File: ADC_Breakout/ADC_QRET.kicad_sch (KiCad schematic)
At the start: 33 parts, among them J1 Screw_Terminal_01x03, J2 Screw_Terminal_01x04, J3 Screw_Terminal_01x04, J4 Screw_Terminal_01x04, J5 Screw_Terminal_01x04, U1 ESP32-S3-DEVKITC-1-N8R2

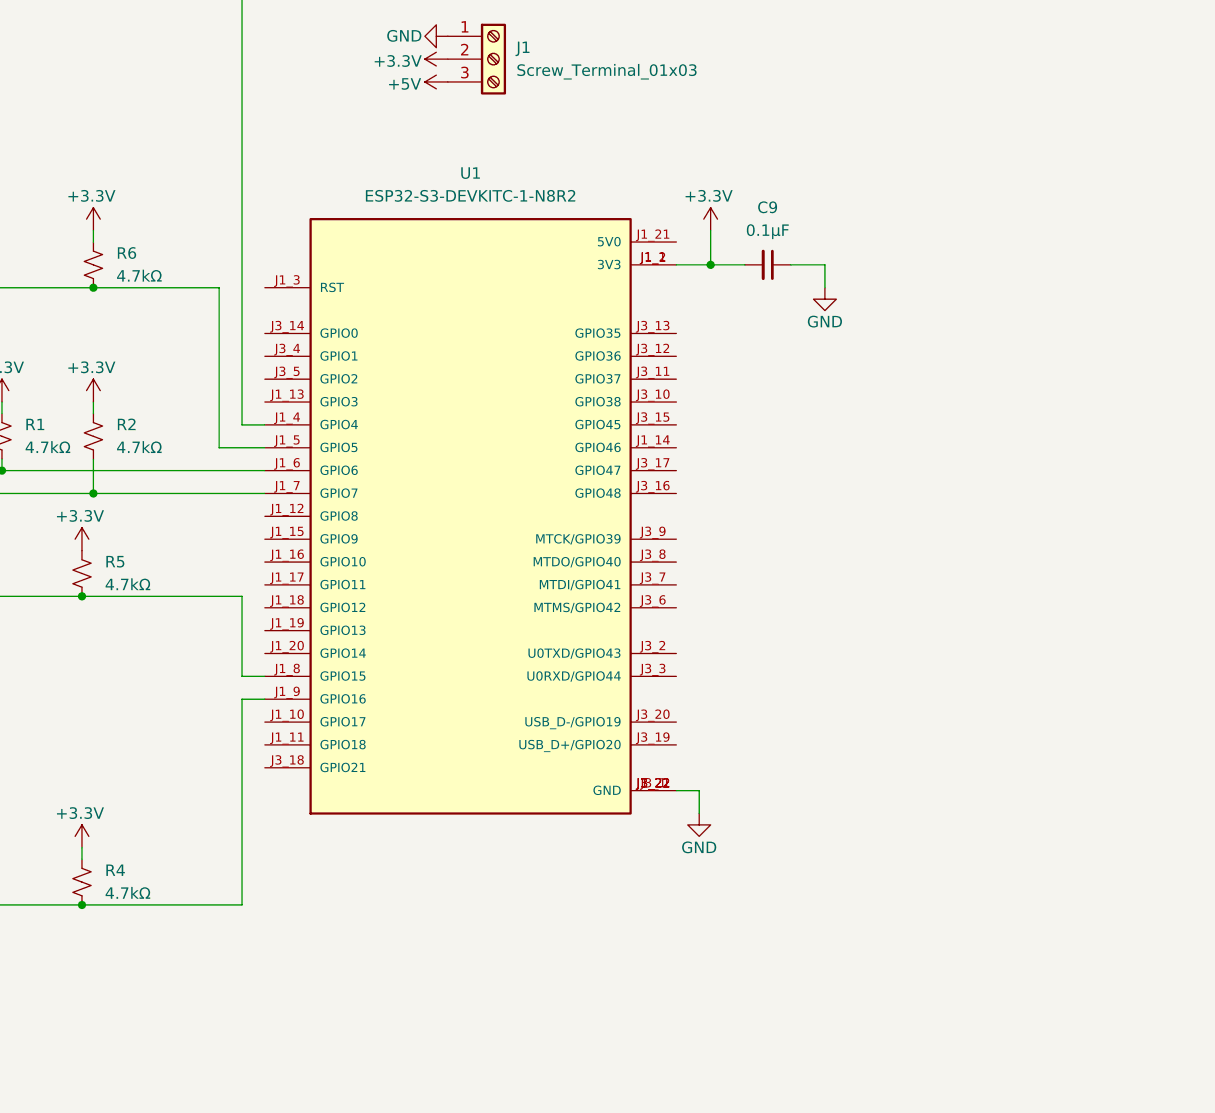
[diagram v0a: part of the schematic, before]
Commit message: Added ESP32 IO Terminals
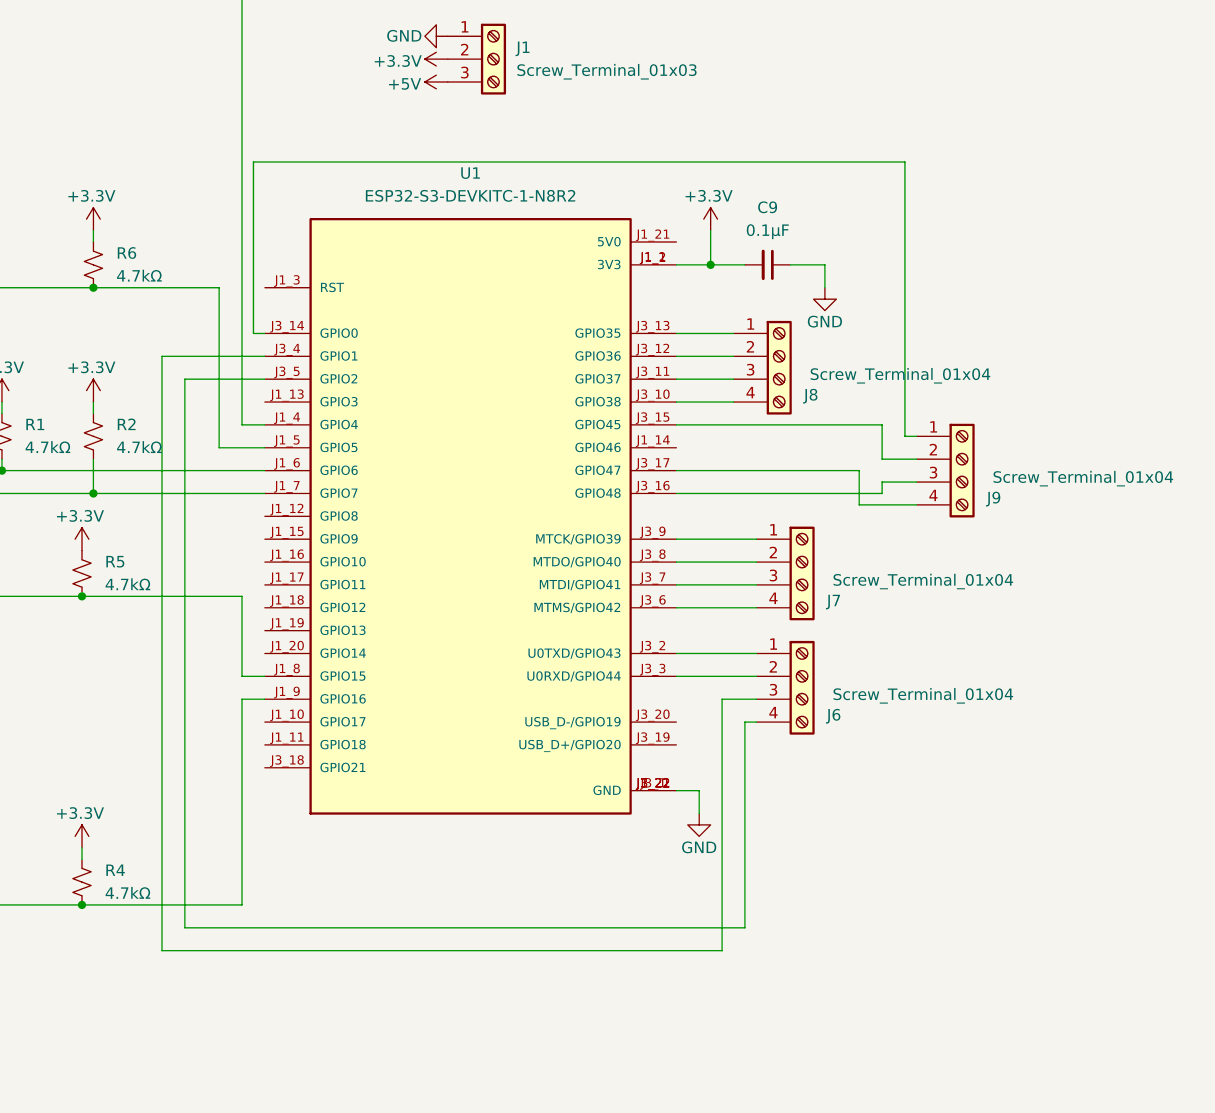
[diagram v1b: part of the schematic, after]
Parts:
- added J6, J7, J8, J9: Screw_Terminal_01x04, TerminalBlock:TerminalBlock_Xinya_XY308-2.54-4P_1x04_P2.54mm_Horizontal, symbol Connector:Screw_Terminal_01x04
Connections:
- net at U1.J3_10 (GPIO38): now also J8.4 (Pin_4)
- net at U1.J3_11 (GPIO37): now also J8.3 (Pin_3)
- net at U1.J3_12 (GPIO36): now also J8.2 (Pin_2)
- net at U1.J3_13 (GPIO35): now also J8.1 (Pin_1)
- net at U1.J3_14 (GPIO0): now also J9.1 (Pin_1)
- net at U1.J3_15 (GPIO45): now also J9.2 (Pin_2)
- net at U1.J3_16 (GPIO48): now also J9.3 (Pin_3)
- net at U1.J3_17 (GPIO47): now also J9.4 (Pin_4)
- net at U1.J3_2 (U0TXD/GPIO43): now also J6.1 (Pin_1)
- net at U1.J3_3 (U0RXD/GPIO44): now also J6.2 (Pin_2)
- net at U1.J3_4 (GPIO1): now also J6.3 (Pin_3)
- net at U1.J3_5 (GPIO2): now also J6.4 (Pin_4)
- net at U1.J3_6 (MTMS/GPIO42): now also J7.4 (Pin_4)
- net at U1.J3_7 (MTDI/GPIO41): now also J7.3 (Pin_3)
- net at U1.J3_8 (MTDO/GPIO40): now also J7.2 (Pin_2)
- net at U1.J3_9 (MTCK/GPIO39): now also J7.1 (Pin_1)
